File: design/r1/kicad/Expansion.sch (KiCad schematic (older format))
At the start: 2 parts

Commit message: Initial cleanup
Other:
- note added: "1"
- note added: "Copyright ©2019-2020 Ross Bamford and Contributors.\nOpen Source Hardware licenced under CERN Open Hardware Licence. \nSee https://github.com/roscopeco/rosco_m68k/blob/master/LICENCE.hardware.txt\nOSHWA UK000006 (https://certification.oshwa.org/uk000006.html)\n"
- note added: "EXPANSION CONNECTOR"
- note removed: "EXPANSION"
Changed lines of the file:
@@
-$EndComp
-$Comp
-L rosco_m68k-eagle-import:A3L-LOC #FRAME5
-U 1 1 52068B2A
-P 1100 10100
-AR Path="/52068B2A" Ref="#FRAME5"  Part="1"
-AR Path="/5E53BC83/52068B2A" Ref="#FRAME5"  Part="1"
-F 0 "#FRAME5" H 1100 10100 50  0001 C CNN
-F 1 "BOOT line generator" H 1100 10100 50  0001 C CNN
-F 2 "" H 1100 10100 50  0001 C CNN
-F 3 "" H 1100 10100 50  0001 C CNN
-	1    1100 10100
-	1    0    0    -1
 $EndComp
 $Comp
@@
 	1    0    0    -1
 $EndComp
-Text Notes 12700 9600 0    170  ~ 0
-EXPANSION
 Text Label 8250 7200 0    50   ~ 0
 D0
@@
 Wire Bus Line
 	10100 2400 7000 2400
+Text Notes 14450 9650 0    59   ~ 0
+Copyright ©2019-2020 Ross Bamford and Contributors.\nOpen Source Hardware licenced under CERN Open Hardware Licence. \nSee https://github.com/roscopeco/rosco_m68k/blob/master/LICENCE.hardware.txt\nOSHWA UK000006 (https://certification.oshwa.org/uk000006.html)\n
+Text Notes 18050 10300 0    59   ~ 0
+1
+Text Notes 14800 10150 0    59   ~ 0
+EXPANSION CONNECTOR
 Wire Bus Line
 	8000 6900 8000 7200

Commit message: Cleanup first pass
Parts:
- added H1, H2, H3, H4: MountingHole, MountingHole:MountingHole_3.2mm_M3, symbol Mechanical:MountingHole
- added IC7: 7404N, rosco_m68k:DIL14, symbol rosco_m68k-eagle-import:7404N
- added IC9: 74LS01N, rosco_m68k:DIL14, symbol rosco_m68k-eagle-import:7401N
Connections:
- net GND: now also IC7.11 (I), IC7.13 (I), IC7.9 (I), IC9.11 (I0), IC9.12 (I1)
- net R/W renamed RW
- no-connect marks 0 -> 4

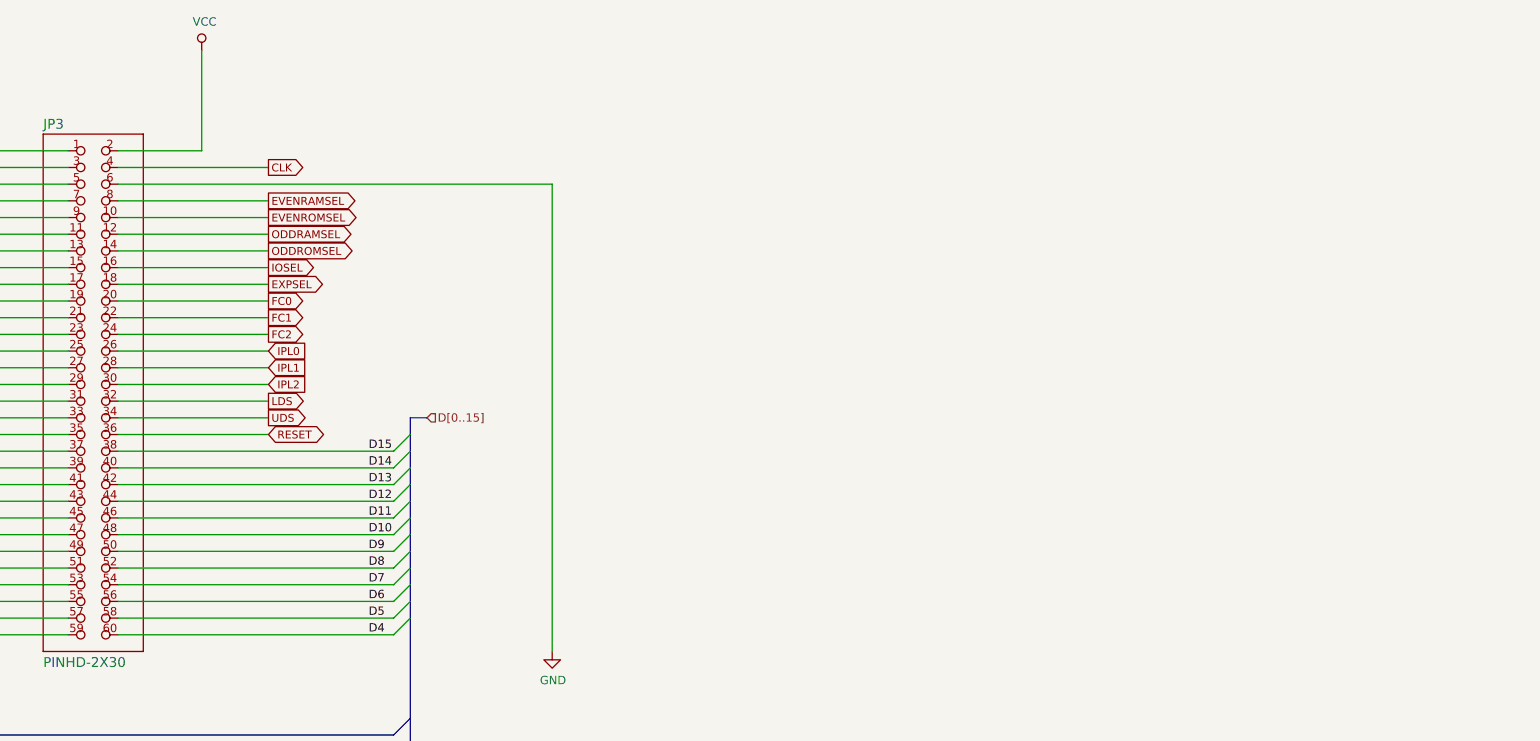
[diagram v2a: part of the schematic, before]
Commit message: GPIO, Legacy Peripheral and Panel support
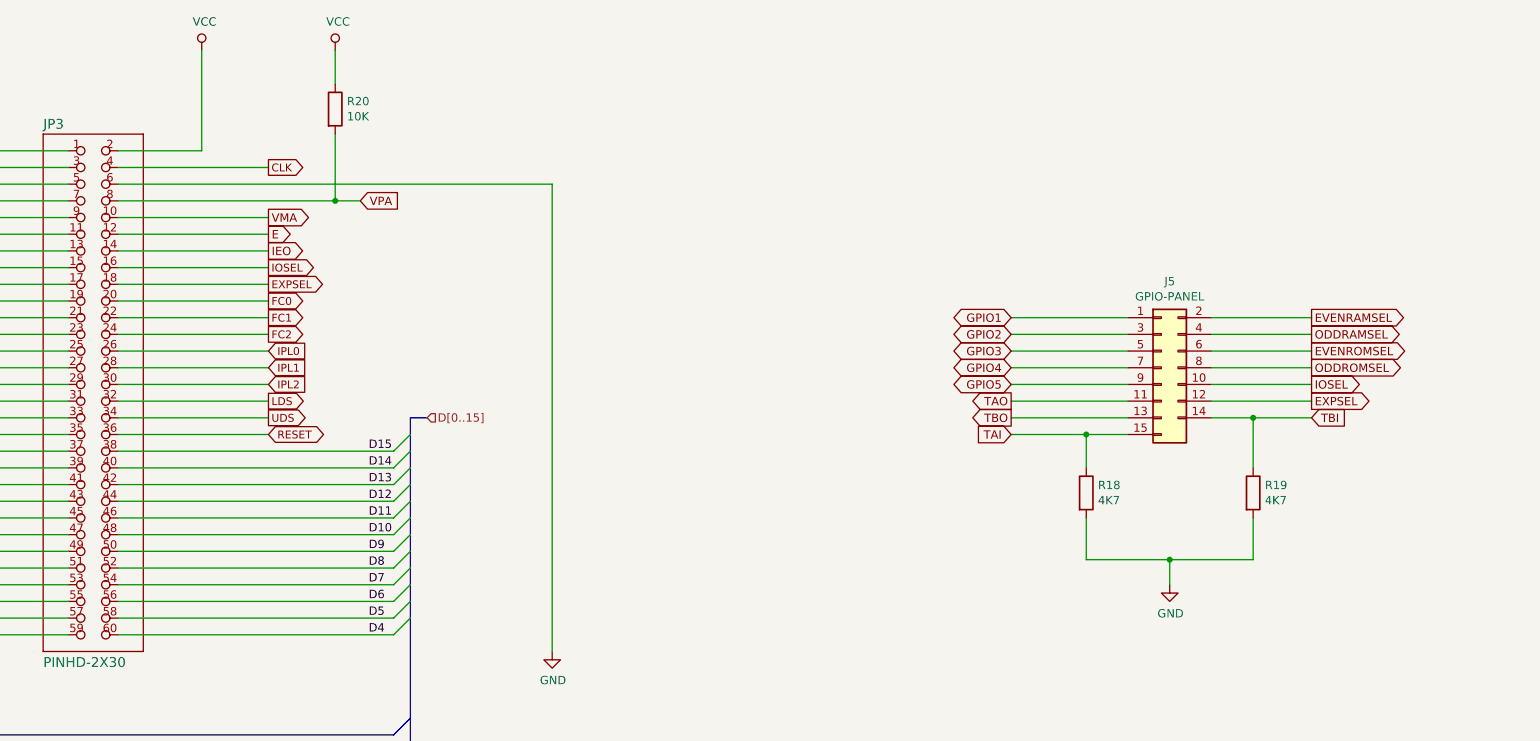
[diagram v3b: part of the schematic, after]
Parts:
- added J5: GPIO-PANEL, symbol Connector_Generic:Conn_2Rows-15Pins
- added R18, R19: 4K7, symbol Device:R
- added R20: 10K, symbol Device:R
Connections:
- net EVENRAMSEL: now also J5.2 (Pin_2); no longer JP3.8
- net EVENROMSEL: now also J5.6 (Pin_6); no longer JP3.10
- net EXPSEL: now also J5.12 (Pin_12)
- net GND: now also R18.2, R19.2
- net IOSEL: now also J5.10 (Pin_10)
- net ODDRAMSEL: now also J5.4 (Pin_4); no longer JP3.12
- net ODDROMSEL: now also J5.8 (Pin_8); no longer JP3.14
- net VCC: now also R20.1
- new net E: JP3.12
- new net GPIO1: J5.1 (Pin_1)
- new net GPIO2: J5.3 (Pin_3)
- new net GPIO3: J5.5 (Pin_5)
- new net GPIO4: J5.7 (Pin_7)
- new net GPIO5: J5.9 (Pin_9)
- new net IEO: JP3.14
- new net TAI: J5.15 (Pin_15), R18.1
- new net TAO: J5.11 (Pin_11)
- new net TBI: J5.14 (Pin_14), R19.1
- new net TBO: J5.13 (Pin_13)
- new net VMA: JP3.10
- new net VPA: JP3.8, R20.2
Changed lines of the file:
@@
 CLK
 Wire Wire Line
-	9900 3700 9000 3700
-Text GLabel 9900 3700 2    47   Output ~ 0
-EVENRAMSEL
-Wire Wire Line
 	9900 3800 9000 3800
-Text GLabel 9900 3800 2    47   Output ~ 0
-EVENROMSEL
 Wire Wire Line
 	9900 3900 9000 3900
-Text GLabel 9900 3900 2    47   Output ~ 0
-ODDRAMSEL
 Wire Wire Line
 	9900 4000 9000 4000
-Text GLabel 9900 4000 2    47   Output ~ 0
-ODDROMSEL
 Wire Wire Line
 	9900 4100 9000 4100
@@
 Wire Wire Line
 	2250 5100 2250 6150
+$Comp
+L Connector_Generic:Conn_2Rows-15Pins J5
+U 1 1 600521A7
+P 15250 4700
+F 0 "J5" H 15300 5217 50  0000 C CNN
+F 1 "GPIO-PANEL" H 15300 5126 50  0000 C CNN
+F 2 "" H 15250 4700 50  0001 C CNN
+F 3 "~" H 15250 4700 50  0001 C CNN
+	1    15250 4700
+	1    0    0    -1
+$EndComp
+Wire Wire Line
+	15050 4400 14350 4400
+Wire Wire Line
+	15050 4500 14350 4500
+Wire Wire Line
+	15050 4600 14350 4600
+Wire Wire Line
+	15050 4700 14350 4700
+Wire Wire Line
+	15050 4800 14350 4800
+Wire Wire Line
+	15050 4900 14350 4900
+Wire Wire Line
+	15050 5000 14350 5000
+Wire Wire Line
+	15050 5100 14800 5100
+Wire Wire Line
+	15550 4500 16150 4500
+Wire Wire Line
+	15550 4600 16150 4600
+Wire Wire Line
+	15550 4700 16150 4700
+Wire Wire Line
+	15550 4800 16150 4800
+Wire Wire Line
+	15550 5000 15800 5000
+Text GLabel 14350 4400 0    50   BiDi ~ 0
+GPIO1
+Text GLabel 14350 4500 0    50   BiDi ~ 0
+GPIO2
+Text GLabel 14350 4600 0    50   BiDi ~ 0
+GPIO3
+Text GLabel 14350 4700 0    50   BiDi ~ 0
+GPIO4
+Text GLabel 14350 4800 0    50   BiDi ~ 0
+GPIO5
+Text GLabel 14350 4900 0    50   Output ~ 0
+TAO
+Text GLabel 14350 5000 0    50   Output ~ 0
+TBO
+Text GLabel 9900 4000 2    50   Output ~ 0
+IEO
+Text GLabel 14350 5100 0    50   Input ~ 0
+TAI
+Text GLabel 16150 5000 2    50   Input ~ 0
+TBI
+Text GLabel 10450 3700 2    50   Input ~ 0
+VPA
+Text GLabel 9900 3800 2    50   Output ~ 0
+VMA
+Text GLabel 9900 3900 2    50   Output ~ 0
+E
+$Comp
+L Device:R R18
+U 1 1 6009D68E
+P 14800 5450
+F 0 "R18" H 14870 5496 50  0000 L CNN
+F 1 "4K7" H 14870 5405 50  0000 L CNN
+F 2 "" V 14730 5450 50  0001 C CNN
+F 3 "~" H 14800 5450 50  0001 C CNN
+	1    14800 5450
+	1    0    0    -1
+$EndComp
+$Comp
+L Device:R R19
+U 1 1 6009E518
+P 15800 5450
+F 0 "R19" H 15870 5496 50  0000 L CNN
+F 1 "4K7" H 15870 5405 50  0000 L CNN
+F 2 "" V 15730 5450 50  0001 C CNN
+F 3 "~" H 15800 5450 50  0001 C CNN
+	1    15800 5450
+	1    0    0    -1
+$EndComp
+$Comp
+L power:GND #PWR0112
+U 1 1 600A0436
+P 15300 6000
+F 0 "#PWR0112" H 15300 5750 50  0001 C CNN
+F 1 "GND" H 15305 5827 50  0000 C CNN
+F 2 "" H 15300 6000 50  0001 C CNN
+F 3 "" H 15300 6000 50  0001 C CNN
+	1    15300 6000
+	1    0    0    -1
+$EndComp
+Wire Wire Line
+	15800 5300 15800 5000
+Connection ~ 15800 5000
+Wire Wire Line
+	15800 5000 16150 5000
+Wire Wire Line
+	15800 5850 15800 5600
+Wire Wire Line
+	15300 6000 15300 5850
+Connection ~ 15300 5850
+Wire Wire Line
+	15300 5850 15800 5850
+$Comp
+L Device:R R20
+U 1 1 600B8632
+P 10300 3150
+F 0 "R20" H 10370 3196 50  0000 L CNN
+F 1 "10K" H 10370 3105 50  0000 L CNN
+F 2 "" V 10230 3150 50  0001 C CNN
+F 3 "~" H 10300 3150 50  0001 C CNN
+	1    10300 3150
+	1    0    0    -1
+$EndComp
+$Comp
+L power:VCC #PWR0154
+U 1 1 600B9802
+P 10300 2800
+F 0 "#PWR0154" H 10300 2650 50  0001 C CNN
+F 1 "VCC" H 10317 2973 50  0000 C CNN
+F 2 "" H 10300 2800 50  0001 C CNN
+F 3 "" H 10300 2800 50  0001 C CNN
+	1    10300 2800
+	1    0    0    -1
+$EndComp
+Wire Wire Line
+	9000 3700 10300 3700
+Wire Wire Line
+	15550 4400 16150 4400
+Wire Wire Line
+	10300 2800 10300 3000
+Wire Wire Line
+	10300 3300 10300 3700
+Connection ~ 10300 3700
+Wire Wire Line
+	10300 3700 10450 3700
+Text GLabel 16150 4400 2    50   Output ~ 0
+EVENRAMSEL
+Text GLabel 16150 4500 2    50   Output ~ 0
+ODDRAMSEL
+Text GLabel 16150 4600 2    50   Output ~ 0
+EVENROMSEL
+Text GLabel 16150 4700 2    50   Output ~ 0
+ODDROMSEL
+Wire Wire Line
+	15550 4900 16150 4900
+Wire Wire Line
+	14800 5850 14800 5600
+Wire Wire Line
+	14800 5850 15300 5850
+Wire Wire Line
+	14800 5300 14800 5100
+Connection ~ 14800 5100
+Wire Wire Line
+	14800 5100 14350 5100
 Wire Bus Line
 	8000 6900 8000 7200
@@
 Wire Bus Line
 	7500 3050 7500 5400
+Text GLabel 16150 4800 2    50   Output ~ 0
+IOSEL
+Text GLabel 16150 4900 2    50   Output ~ 0
+EXPSEL
 $EndSCHEMATC

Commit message: Design complete
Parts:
- J5: footprint (none) -> Connector_PinHeader_2.54mm:PinHeader_2x08_P2.54mm_Vertical
- R1: renamed from R20; footprint (none) -> rosco_m68k:0207_10
- R18, R19: footprint (none) -> rosco_m68k:0207_10
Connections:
- net E: now also JP3.10; no longer JP3.12
- net VMA: now also JP3.12; no longer JP3.10
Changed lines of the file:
@@
 F 0 "J5" H 15300 5217 50  0000 C CNN
 F 1 "GPIO-PANEL" H 15300 5126 50  0000 C CNN
-F 2 "" H 15250 4700 50  0001 C CNN
+F 2 "Connector_PinHeader_2.54mm:PinHeader_2x08_P2.54mm_Vertical" H 15250 4700 50  0001 C CNN
 F 3 "~" H 15250 4700 50  0001 C CNN
 	1    15250 4700
@@
 Text GLabel 10450 3700 2    50   Input ~ 0
 VPA
+Text GLabel 9900 3900 2    50   Output ~ 0
+VMA
 Text GLabel 9900 3800 2    50   Output ~ 0
-VMA
-Text GLabel 9900 3900 2    50   Output ~ 0
 E
 $Comp
@@
 F 0 "R18" H 14870 5496 50  0000 L CNN
 F 1 "4K7" H 14870 5405 50  0000 L CNN
-F 2 "" V 14730 5450 50  0001 C CNN
+F 2 "rosco_m68k:0207_10" V 14730 5450 50  0001 C CNN
 F 3 "~" H 14800 5450 50  0001 C CNN
 	1    14800 5450
@@
 F 0 "R19" H 15870 5496 50  0000 L CNN
 F 1 "4K7" H 15870 5405 50  0000 L CNN
-F 2 "" V 15730 5450 50  0001 C CNN
+F 2 "rosco_m68k:0207_10" V 15730 5450 50  0001 C CNN
 F 3 "~" H 15800 5450 50  0001 C CNN
 	1    15800 5450
@@
 	15300 5850 15800 5850
 $Comp
-L Device:R R20
+L Device:R R1
 U 1 1 600B8632
 P 10300 3150
-F 0 "R20" H 10370 3196 50  0000 L CNN
+F 0 "R1" H 10370 3196 50  0000 L CNN
 F 1 "10K" H 10370 3105 50  0000 L CNN
-F 2 "" V 10230 3150 50  0001 C CNN
+F 2 "rosco_m68k:0207_10" V 10230 3150 50  0001 C CNN
 F 3 "~" H 10300 3150 50  0001 C CNN
 	1    10300 3150
@@
 Wire Wire Line
 	14800 5100 14350 5100
+Text GLabel 16150 4800 2    50   Output ~ 0
+IOSEL
+Text GLabel 16150 4900 2    50   Output ~ 0
+EXPSEL
 Wire Bus Line
 	8000 6900 8000 7200
@@
 Wire Bus Line
 	7500 3050 7500 5400
-Text GLabel 16150 4800 2    50   Output ~ 0
-IOSEL
-Text GLabel 16150 4900 2    50   Output ~ 0
-EXPSEL
 $EndSCHEMATC

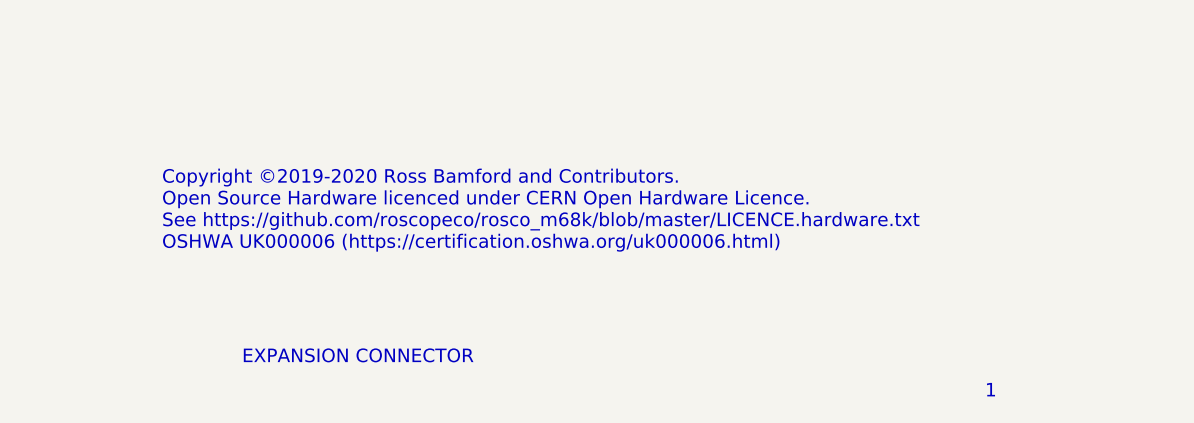
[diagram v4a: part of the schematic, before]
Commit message: Fix #18 and apply suggestions from #17
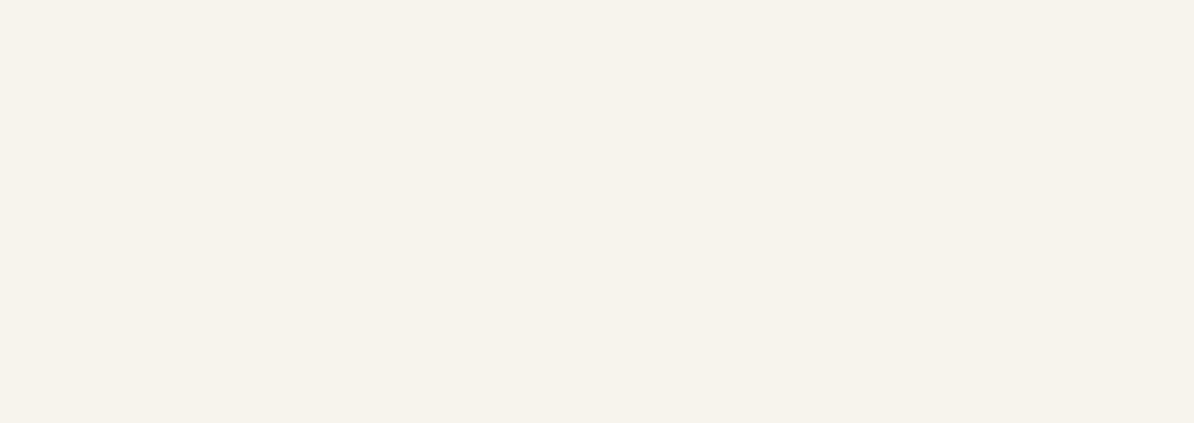
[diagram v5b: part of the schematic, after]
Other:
- note removed: "1"
- note removed: "Copyright ©2019-2020 Ross Bamford and Contributors.\nOpen Source Hardware licenced under CERN Open Hardware Licence. \nSee https://github.com/roscopeco/rosco_m68k/blob/master/LICENCE.hardware.txt\nOSHWA UK000006 (https://certification.oshwa.org/uk000006.html)\n"
- note removed: "EXPANSION CONNECTOR"
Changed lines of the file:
@@
 encoding utf-8
 Sheet 6 6
-Title ""
+Title "EXPANSION AND IO"
 Date "2020-02-25"
-Rev ""
+Rev "1"
 Comp ""
-Comment1 ""
-Comment2 ""
-Comment3 ""
-Comment4 ""
+Comment1 "OSHWA UK000006 (https://certification.oshwa.org/uk000006.html)"
+Comment2 "See https://github.com/roscopeco/rosco_m68k/blob/master/LICENCE.hardware.txt"
+Comment3 "Open Source Hardware licenced under CERN Open Hardware Licence"
+Comment4 "Copyright 2019-2020 Ross Bamford and Contributors"
 $EndDescr
 Wire Wire Line
@@
 Wire Bus Line
 	7400 3050 7500 3050
-Text Notes 14450 9650 0    59   ~ 0
-Copyright ©2019-2020 Ross Bamford and Contributors.\nOpen Source Hardware licenced under CERN Open Hardware Licence. \nSee https://github.com/roscopeco/rosco_m68k/blob/master/LICENCE.hardware.txt\nOSHWA UK000006 (https://certification.oshwa.org/uk000006.html)\n
-Text Notes 18050 10300 0    59   ~ 0
-1
 Wire Wire Line
 	9000 5200 10650 5200
@@
 	1    0    0    -1
 $EndComp
-Text Notes 14800 10150 0    59   ~ 0
-EXPANSION CONNECTOR
 Wire Wire Line
 	2350 3200 2250 3200
